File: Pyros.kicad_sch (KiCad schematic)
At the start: 38 parts, among them J1 PYRO_XT60, J7 J_PYRO1, J8 J_PYRO2, Q1 AO3400A, Q3 AO3400A, Q5 AO3401A, U10 PC817, U11 PC817, U9 PC817

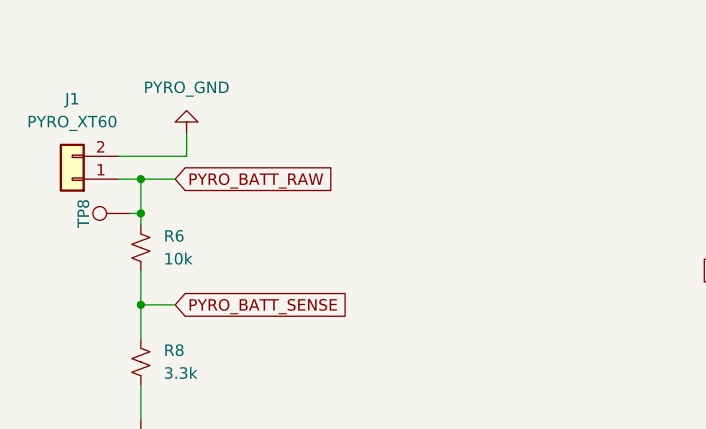
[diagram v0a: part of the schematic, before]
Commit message: feat: finish schematic (erc_pass)
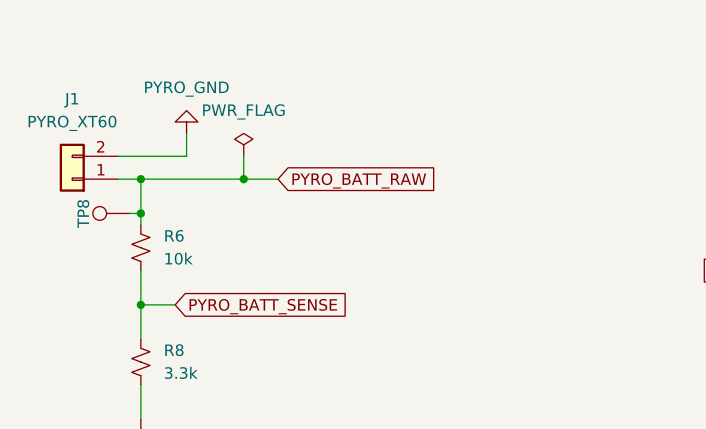
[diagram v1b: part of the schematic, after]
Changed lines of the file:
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@@
 	)
 	(junction
-		(at 30.48 48.26)
-		(diameter 0)
-		(color 0 0 0 0)
-	)
-	(junction
 		(at 146.05 55.88)
 		(diameter 0)
@@
 	)
 	(junction
+		(at 41.91 48.26)
+		(diameter 0)
+		(color 0 0 0 0)
+	)
+	(junction
 		(at 243.84 71.12)
 		(diameter 0)
@@
 	)
 	(junction
+		(at 30.48 48.26)
+		(diameter 0)
+		(color 0 0 0 0)
+	)
+	(junction
 		(at 146.05 76.2)
 		(diameter 0)
@@
 	(wire
 		(pts
+			(xy 41.91 48.26) (xy 45.72 48.26)
+		)
+		(stroke
+			(width 0)
+			(type default)
+		)
+	)
+	(wire
+		(pts
 			(xy 146.05 43.18) (xy 146.05 50.8)
 		)
@@
 	(wire
 		(pts
+			(xy 41.91 45.72) (xy 41.91 48.26)
+		)
+		(stroke
+			(width 0)
+			(type default)
+		)
+	)
+	(wire
+		(pts
 			(xy 233.68 63.5) (xy 233.68 66.04)
 		)
@@
 	(wire
 		(pts
-			(xy 30.48 48.26) (xy 34.29 48.26)
+			(xy 30.48 48.26) (xy 41.91 48.26)
 		)
 		(stroke
@@
 	(global_label "PYRO_BATT_RAW"
 		(shape input)
-		(at 34.29 48.26 0)
+		(at 45.72 48.26 0)
 		(fields_autoplaced yes)
 		(effects
@@
 		)
 		(property "Intersheetrefs" "${INTERSHEET_REFS}"
-			(at 52.2733 48.26 0)
+			(at 63.7033 48.26 0)
 			(hide yes)
 			(show_name no)
@@
 					(unit 1)
 				)
+			)
+		)
+	)
+	(symbol
+		(lib_id "power:PWR_FLAG")
+		(at 41.91 45.72 0)
+		(unit 1)
+		(body_style 1)
+		(exclude_from_sim no)
+		(in_bom yes)
+		(on_board yes)
+		(in_pos_files yes)
+		(dnp no)
+		(fields_autoplaced yes)
+		(property "Reference" "#FLG02"
+			(at 41.91 43.815 0)
+			(hide yes)
+			(show_name no)
+			(do_not_autoplace no)
+			(effects
+				(font
+					(size 1.27 1.27)
+				)
+			)
+		)
+		(property "Value" "PWR_FLAG"
+			(at 41.91 40.64 0)
+			(show_name no)
+			(do_not_autoplace no)
+			(effects
+				(font
+					(size 1.27 1.27)
+				)
+			)
+		)
+		(property "Footprint" ""
+			(at 41.91 45.72 0)
+			(hide yes)
+			(show_name no)
+			(do_not_autoplace no)
+			(effects
+				(font
+					(size 1.27 1.27)
+				)
+			)
+		)
+		(property "Datasheet" ""
+			(at 41.91 45.72 0)
+			(hide yes)
+			(show_name no)
+			(do_not_autoplace no)
+			(effects
+				(font
+					(size 1.27 1.27)
+				)
+			)
+		)
+		(property "Description" "Special symbol for telling ERC where power comes from"
+			(at 41.91 45.72 0)
+			(hide yes)
+			(show_name no)
+			(do_not_autoplace no)
+			(effects
+				(font
+					(size 1.27 1.27)
+				)
+			)
+		)
+		(pin "1"
+		)
+		(instances
+			(project "UNSW_Rocketry_Senior_Flight_Computer"
+				(path "/9e0253f5-fba5-4205-8256-7fc47a91dd1e/810ac388-79e0-4279-a05f-a2a0b85dc963"
+					(reference "#FLG02")
+					(unit 1)
+				)

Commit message: feat: finish schematic (Full)
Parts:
- D10: value LED -> LED_YELLOW
- D12: renamed from D11; value LED -> LED_YELLOW
- D9: renamed from D13; value LED -> LED_RED
- renumbered D9 to D11, D12 to D13, J1 to J6, Q5 to Q2, Q1 to Q3, Q3 to Q4, R6 to R15, R8 to R16, R10 to R17, R29 to R18, R30 to R19, R11 to R20, R28 to R21, R14 to R22, R18 to R23, R22 to R24, R20 to R25, R21 to R26, R19 to R27, R23 to R28, R24 to R29, R25 to R30, R26 to R31, R27 to R32, TP1 to TP10, TP12 to TP11, TP2 to TP12, TP11 to TP9, U9 to U10, U10 to U11, U11 to U9

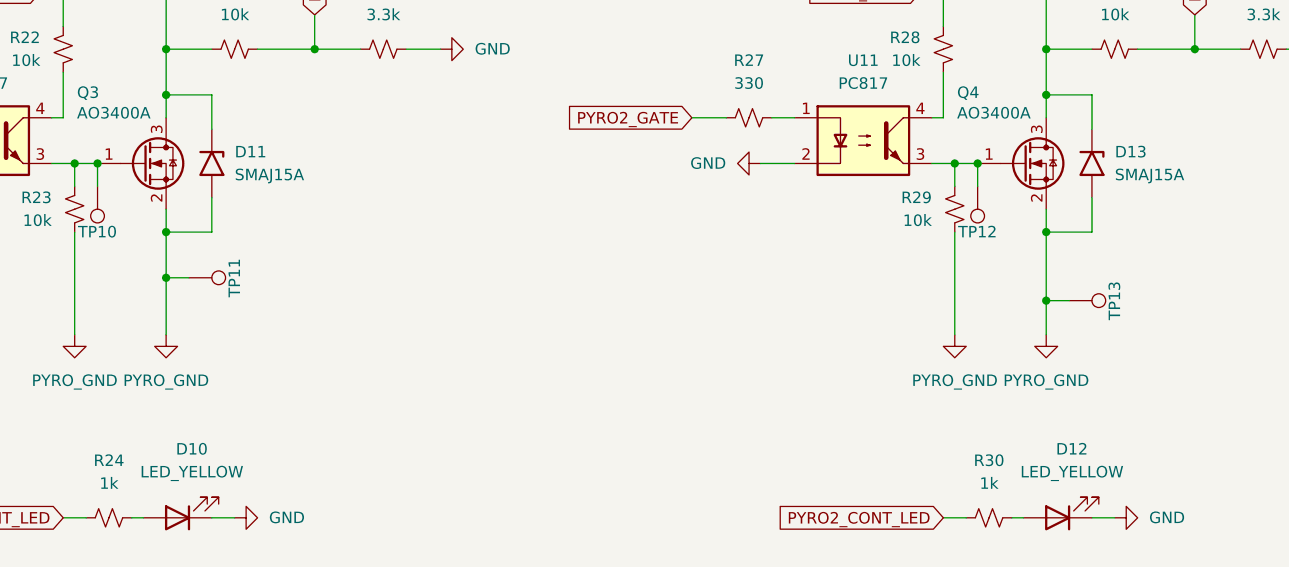
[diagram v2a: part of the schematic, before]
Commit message: feat: PCB Designed (Silk screen adjustments)
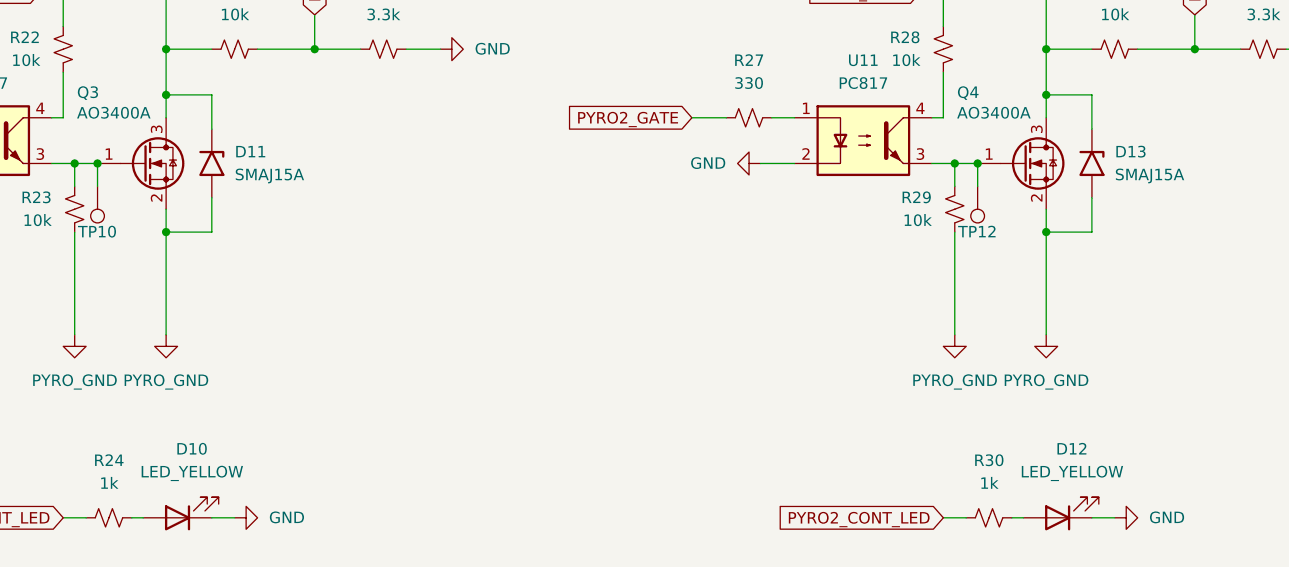
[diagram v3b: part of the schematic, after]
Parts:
- removed TP11, TP13: 1.0mm, PCM_SparkFun-Connector:TestPoint-1.0mm, symbol PCM_SparkFun-Connector:TestPoint_1.0mm
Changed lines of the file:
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@@
 	)
 	(junction
-		(at 243.84 78.74)
-		(diameter 0)
-		(color 0 0 0 0)
-	)
-	(junction
 		(at 134.62 44.45)
 		(diameter 0)
@@
 	)
 	(junction
-		(at 146.05 76.2)
-		(diameter 0)
-		(color 0 0 0 0)
-	)
-	(junction
 		(at 138.43 63.5)
 		(diameter 0)
@@
 	(wire
 		(pts
-			(xy 146.05 76.2) (xy 146.05 82.55)
-		)
-		(stroke
-			(width 0)
-			(type default)
-		)
-	)
-	(wire
-		(pts
 			(xy 133.35 158.75) (xy 133.35 160.02)
 		)
@@
 	(wire
 		(pts
-			(xy 243.84 78.74) (xy 243.84 82.55)
-		)
-		(stroke
-			(width 0)
-			(type default)
-		)
-	)
-	(wire
-		(pts
 			(xy 151.13 102.87) (xy 153.67 102.87)
 		)
@@
 	(wire
 		(pts
-			(xy 243.84 78.74) (xy 246.38 78.74)
-		)
-		(stroke
-			(width 0)
-			(type default)
-		)
-	)
-	(wire
-		(pts
 			(xy 135.89 63.5) (xy 138.43 63.5)
 		)
@@
 	(wire
 		(pts
-			(xy 146.05 71.12) (xy 146.05 76.2)
+			(xy 146.05 71.12) (xy 146.05 82.55)
 		)
 		(stroke
@@
 	(wire
 		(pts
-			(xy 243.84 71.12) (xy 243.84 78.74)
+			(xy 243.84 71.12) (xy 243.84 82.55)
 		)
 		(stroke
@@
 	(wire
 		(pts
-			(xy 146.05 76.2) (xy 148.59 76.2)
-		)
-		(stroke
-			(width 0)
-			(type default)
-		)
-	)
-	(wire
-		(pts
 			(xy 260.35 46.99) (xy 260.35 50.8)
 		)
@@
 	)
 	(symbol
-		(lib_id "PCM_SparkFun-Connector:TestPoint_1.0mm")
-		(at 148.59 76.2 270)
-		(unit 1)
-		(body_style 1)
-		(exclude_from_sim no)
-		(in_bom yes)
-		(on_board yes)
-		(in_pos_files yes)
-		(dnp no)
-		(fields_autoplaced yes)
-		(property "Reference" "TP11"
-			(at 153.67 76.2 0)
-			(show_name no)
-			(do_not_autoplace yes)
-			(effects
-				(font
-					(size 1.27 1.27)
-				)
-			)
-		)
-		(property "Value" "1.0mm"
-			(at 144.78 76.2 0)
-			(hide yes)
-			(show_name no)
-			(do_not_autoplace no)
-			(effects
-				(font
-					(size 1.27 1.27)
-				)
-			)
-		)
-		(property "Footprint" "PCM_SparkFun-Connector:TestPoint-1.0mm"
-			(at 142.24 76.2 0)
-			(hide yes)
-			(show_name no)
-			(do_not_autoplace no)
-			(effects
-				(font
-					(size 1.27 1.27)
-				)
-			)
-		)
-		(property "Datasheet" ""
-			(at 140.97 76.2 0)
-			(hide yes)
-			(show_name no)
-			(do_not_autoplace no)
-			(effects
-				(font
-					(size 1.27 1.27)
-				)
-			)
-		)
-		(property "Description" "Test Point"
-			(at 138.43 76.2 0)
-			(hide yes)
-			(show_name no)
-			(do_not_autoplace no)
-			(effects
-				(font
-					(size 1.27 1.27)
-				)
-			)
-		)
-		(pin "1"
-		)
-		(instances
-			(project "UNSW_Rocketry_Senior_Flight_Computer"
-				(path "/9e0253f5-fba5-4205-8256-7fc47a91dd1e/810ac388-79e0-4279-a05f-a2a0b85dc963"
-					(reference "TP11")
-					(unit 1)
-				)
-			)
-		)
-	)
-	(symbol
 		(lib_id "Diode:SMAJ15A")
 		(at 248.92 63.5 270)
@@
 					(unit 1)
 				)
-			)
-		)
-	)
-	(symbol
-		(lib_id "PCM_SparkFun-Connector:TestPoint_1.0mm")
-		(at 246.38 78.74 270)
-		(unit 1)
-		(body_style 1)
-		(exclude_from_sim no)
-		(in_bom yes)
-		(on_board yes)
-		(in_pos_files yes)
-		(dnp no)
-		(fields_autoplaced yes)
-		(property "Reference" "TP13"
-			(at 251.46 78.74 0)
-			(show_name no)
-			(do_not_autoplace yes)
-			(effects
-				(font
-					(size 1.27 1.27)
-				)
-			)
-		)
-		(property "Value" "1.0mm"
-			(at 242.57 78.74 0)
-			(hide yes)
-			(show_name no)
-			(do_not_autoplace no)
-			(effects
-				(font
-					(size 1.27 1.27)
-				)
-			)
-		)
-		(property "Footprint" "PCM_SparkFun-Connector:TestPoint-1.0mm"
-			(at 240.03 78.74 0)
-			(hide yes)
-			(show_name no)
-			(do_not_autoplace no)
-			(effects
-				(font
-					(size 1.27 1.27)
-				)
-			)
-		)
-		(property "Datasheet" ""
-			(at 238.76 78.74 0)
-			(hide yes)
-			(show_name no)
-			(do_not_autoplace no)
-			(effects
-				(font
-					(size 1.27 1.27)
-				)
-			)
-		)
-		(property "Description" "Test Point"
-			(at 236.22 78.74 0)
-			(hide yes)
-			(show_name no)
-			(do_not_autoplace no)
-			(effects
-				(font
-					(size 1.27 1.27)
-				)
-			)
-		)
-		(pin "1"
-		)
-		(instances
-			(project "UNSW_Rocketry_Senior_Flight_Computer"
-				(path "/9e0253f5-fba5-4205-8256-7fc47a91dd1e/810ac388-79e0-4279-a05f-a2a0b85dc963"
-					(reference "TP13")
-					(unit 1)
-				)
